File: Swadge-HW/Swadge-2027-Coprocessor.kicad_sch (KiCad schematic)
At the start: 2 parts, among them U6 CH32V003F4U6

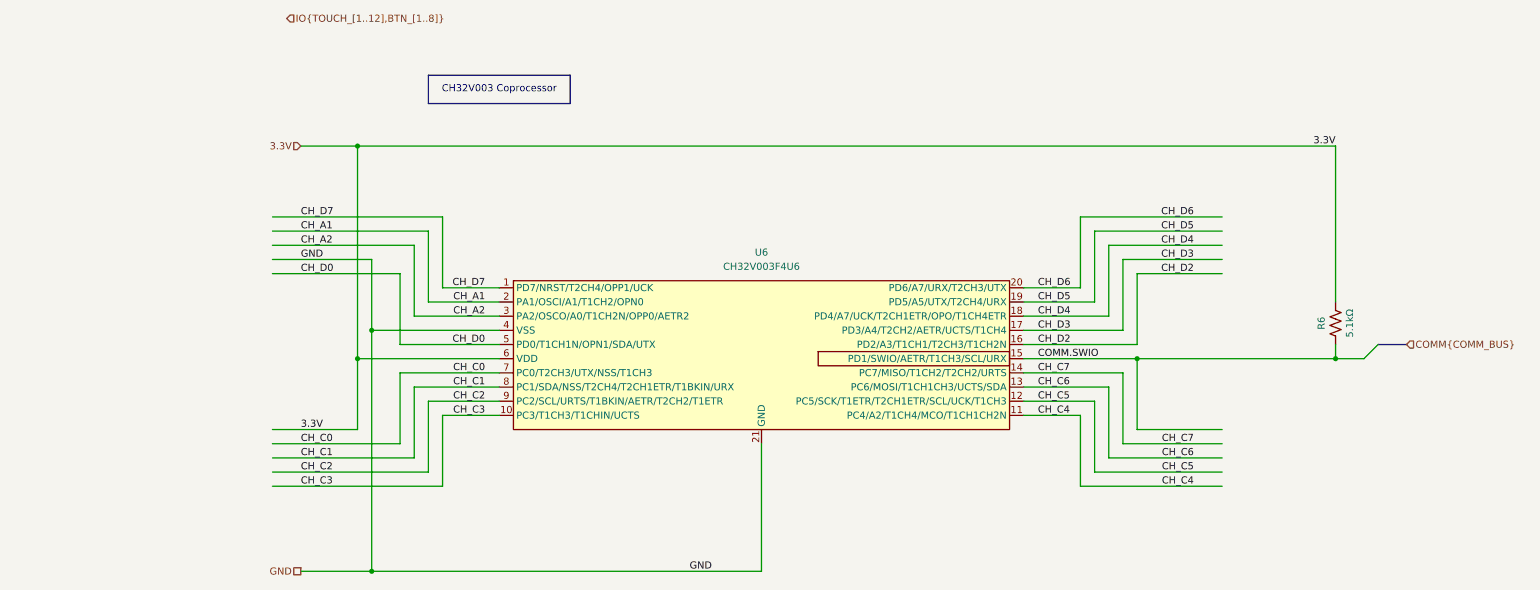
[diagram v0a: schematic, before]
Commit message: Bus Renames
Since we really don't have that many signals I just ditched the bus prefixes and Alias'd them directly.
Added a bus for the interupt and status signals even if they are never used.
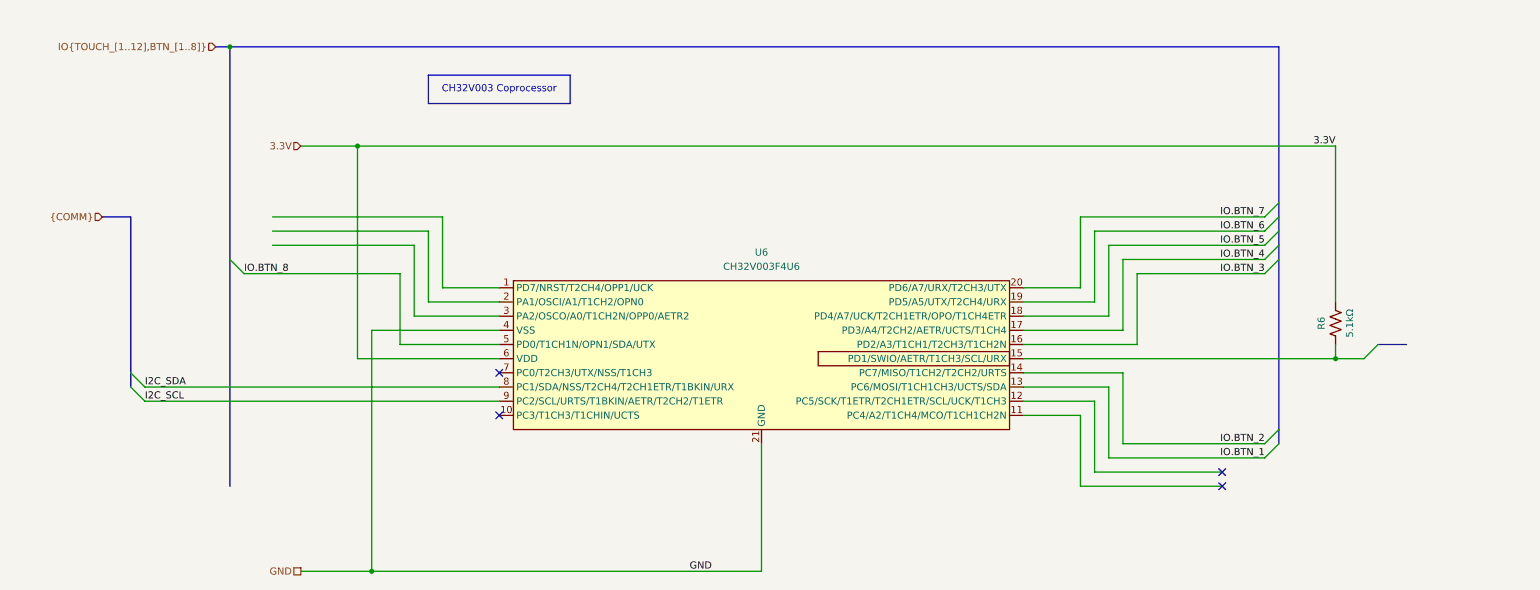
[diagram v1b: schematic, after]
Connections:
- net CH_A1: no longer names the net of U6.2 (PA1/OSCI/A1/T1CH2/OPN0)
- net CH_A2: no longer names the net of U6.3 (PA2/OSCO/A0/T1CH2N/OPP0/AETR2)
- net CH_C0: no longer names the net of U6.7 (PC0/T2CH3/UTX/NSS/T1CH3)
- net CH_C1 renamed I2C_SDA
- net CH_C2 renamed I2C_SCL
- net CH_C3: no longer names the net of U6.10 (PC3/T1CH3/T1CHIN/UCTS)
- net CH_C4: no longer names the net of U6.11 (PC4/A2/T1CH4/MCO/T1CH1CH2N)
- net CH_C5: no longer names the net of U6.12 (PC5/SCK/T1ETR/T2CH1ETR/SCL/UCK/T1CH3)
- net CH_C6 renamed IO.BTN_1
- net CH_C7 renamed IO.BTN_2
- net CH_D0 renamed IO.BTN_8
- net CH_D2 renamed IO.BTN_3
- net CH_D3 renamed IO.BTN_4
- net CH_D4 renamed IO.BTN_5
- net CH_D5 renamed IO.BTN_6
- net CH_D6 renamed IO.BTN_7
- net CH_D7: no longer names the net of U6.1 (PD7/NRST/T2CH4/OPP1/UCK)
- net COMM.SWIO: no longer names the net of R6.1, U6.15 (PD1/SWIO/AETR/T1CH3/SCL/URX)
- no-connect marks 0 -> 4

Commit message: Annotations
Updated Annotations with zonal numbering
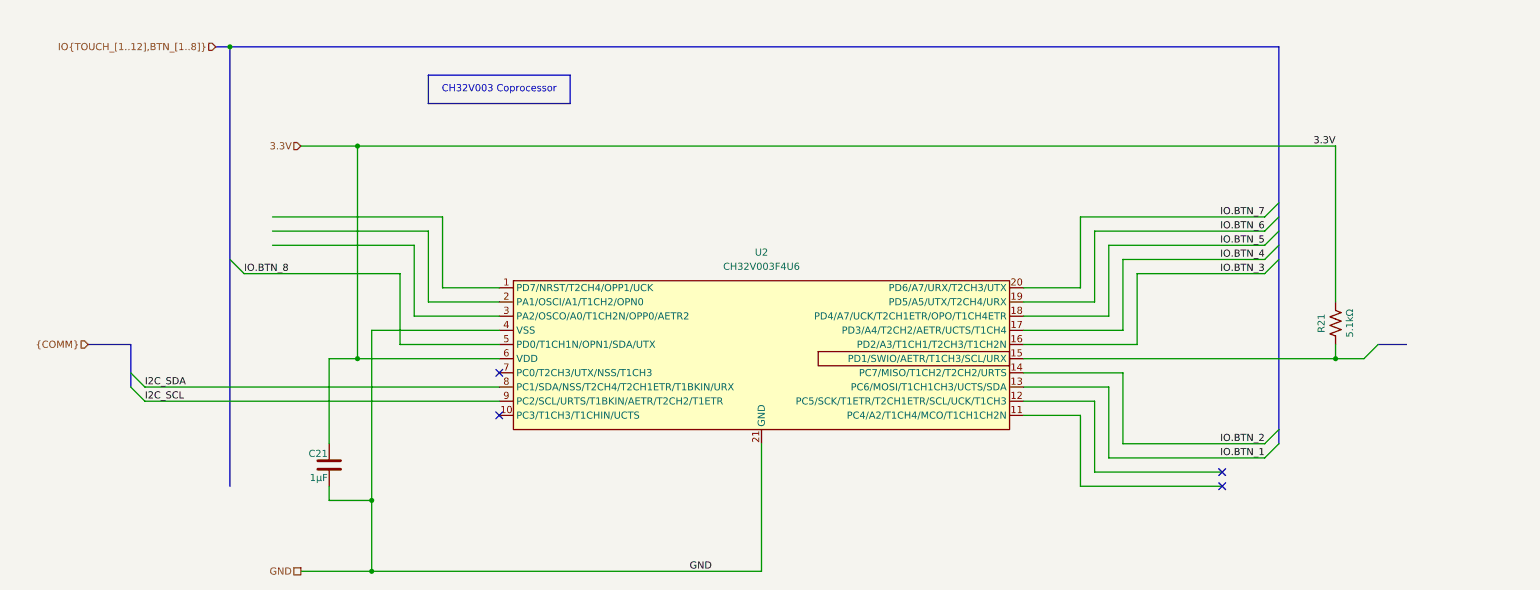
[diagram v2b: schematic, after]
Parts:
- added C21: 1μF, Swadge_Parts:C_0603_1608Metric, symbol Swadge_Parts:C
- renumbered R6 to R21, U6 to U2
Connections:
- net 3.3V: now also C21.1
- net GND: now also C21.2
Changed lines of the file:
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@@
+	)
+	(junction
+		(at 71.12 91.44)
+		(diameter 0)
+		(color 0 0 0 0)
+	)
+	(junction
+		(at 73.66 116.84)
+		(diameter 0)
+		(color 0 0 0 0)
 	)
 	(junction
@@
 	(wire
 		(pts
+			(xy 66.04 91.44) (xy 71.12 91.44)
+		)
+		(stroke
+			(width 0)
+			(type default)
+		)
+	)
+	(wire
+		(pts
 			(xy 208.28 106.68) (xy 233.68 106.68)
 		)
@@
 	(bus
 		(pts
-			(xy 25.4 66.04) (xy 30.48 66.04)
+			(xy 22.86 88.9) (xy 30.48 88.9)
 		)
 		(stroke
@@
 	(wire
 		(pts
-			(xy 73.66 129.54) (xy 73.66 86.36)
+			(xy 73.66 129.54) (xy 73.66 116.84)
+		)
+		(stroke
+			(width 0)
+			(type default)
+		)
+	)
+	(wire
+		(pts
+			(xy 66.04 106.68) (xy 66.04 91.44)
 		)
 		(stroke
@@
 		)
 	)
+	(wire
+		(pts
+			(xy 73.66 116.84) (xy 73.66 86.36)
+		)
+		(stroke
+			(width 0)
+			(type default)
+		)
+	)
+	(wire
+		(pts
+			(xy 66.04 114.3) (xy 66.04 116.84)
+		)
+		(stroke
+			(width 0)
+			(type default)
+		)
+	)
+	(wire
+		(pts
+			(xy 66.04 116.84) (xy 73.66 116.84)
+		)
+		(stroke
+			(width 0)
+			(type default)
+		)
+	)
 	(bus
 		(pts
-			(xy 30.48 66.04) (xy 30.48 93.98)
+			(xy 30.48 88.9) (xy 30.48 93.98)
 		)
 		(stroke
@@
 	(hierarchical_label "{COMM}"
 		(shape input)
-		(at 25.4 66.04 180)
+		(at 22.86 88.9 180)
 		(effects
 			(font
@@
 		(dnp no)
 		(fields_autoplaced yes)
-		(property "Reference" "U6"
+		(property "Reference" "U2"
 			(at 143.51 72.39 0)
 			(show_name no)
@@
 			(project "Swadge-HW"
 				(path "/770c762f-3a30-4864-b7da-de353459cdd6/458cf1f1-40cc-4d0b-81d6-21bbc131062c"
-					(reference "U6")
+					(reference "U2")
+					(unit 1)
+				)
+			)
+		)
+	)
+	(symbol
+		(lib_name "C_13")
+		(lib_id "Swadge_Parts:C")
+		(at 66.04 110.49 0)
+		(mirror y)
+		(unit 1)
+		(body_style 1)
+		(exclude_from_sim no)
+		(in_bom yes)
+		(on_board yes)
+		(in_pos_files yes)
+		(dnp no)
+		(property "Reference" "C21"
+			(at 65.786 108.4579 0)
+			(show_name no)
+			(do_not_autoplace no)
+			(effects
+				(font
+					(size 1.27 1.27)
+				)
+				(justify left)
+			)
+		)
+		(property "Value" "1μF"
+			(at 65.786 112.7759 0)
+			(show_name no)
+			(do_not_autoplace no)
+			(effects
+				(font
+					(size 1.27 1.27)
+				)
+				(justify left)
+			)
+		)
+		(property "Footprint" "Swadge_Parts:C_0603_1608Metric"
+			(at 65.0748 114.3 0)
+			(hide yes)
+			(show_name no)
+			(do_not_autoplace no)
+			(effects
+				(font
+					(size 1.27 1.27)
+				)
+			)
+		)
+		(property "Datasheet" ""
+			(at 66.04 110.49 0)
+			(hide yes)
+			(show_name no)
+			(do_not_autoplace no)
+			(effects
+				(font
+					(size 1.27 1.27)
+				)
+			)
+		)
+		(property "Description" "Unpolarized capacitor"
+			(at 66.04 110.49 0)
+			(hide yes)
+			(show_name no)
+			(do_not_autoplace no)
+			(effects
+				(font
+					(size 1.27 1.27)
+				)
+			)
+		)
+		(property "Digikey" ""
+			(at 62.865 105.41 0)
+			(hide yes)
+			(show_name no)
+			(do_not_autoplace no)
+			(effects
+				(font
+					(size 1.27 1.27)
+				)
+			)
+		)
+		(property "Substitutable" "Y"
+			(at 66.04 110.49 0)
+			(hide yes)
+			(show_name no)
+			(do_not_autoplace no)
+			(effects
+				(font
+					(size 0.001 0.001)
+				)
+			)
+		)
+		(property "LCSC" "C29936"
+			(at 66.04 110.49 0)
+			(hide yes)
+			(show_name no)
+			(do_not_autoplace no)
+			(effects
+				(font
+					(size 1.27 1.27)
+				)
+			)
+		)
+		(pin "2"
+		)
+		(pin "1"
+		)
+		(instances
+			(project "Swadge-HW"
+				(path "/770c762f-3a30-4864-b7da-de353459cdd6/458cf1f1-40cc-4d0b-81d6-21bbc131062c"
+					(reference "C21")
 					(unit 1)
 				)
@@
 		(in_pos_files yes)
 		(dnp no)
-		(property "Reference" "R6"
+		(property "Reference" "R21"
 			(at 243.84 85.09 90)
 			(show_name no)
@@
 			(project "Swadge-HW"
 				(path "/770c762f-3a30-4864-b7da-de353459cdd6/458cf1f1-40cc-4d0b-81d6-21bbc131062c"
-					(reference "R6")
+					(reference "R21")
 					(unit 1)
 				)

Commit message: Starting PCB
Very Rough Initial Layout
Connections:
- no-connect marks 4 -> 7
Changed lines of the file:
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@@
+	)
+	(no_connect
+		(at 55.88 68.58)
+	)
+	(no_connect
+		(at 55.88 71.12)
 	)
 	(no_connect
@@
 	)
 	(no_connect
+		(at 55.88 66.04)
+	)
+	(no_connect

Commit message: major routing changes
Routed SPI
Started Test Routing Touch Inputs
Rough routing for LCD Power
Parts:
- C21: Cost @ 2.5k (none) -> 0.0121
- R21: Cost @ 2.5k 0.0007 -> 0.0023
- U2: Cost @ 2.5k (none) -> 0.1798
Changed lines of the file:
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@@
+			)
+		)
+		(property "Cost @ 2.5k" "0.1798"
+			(at 143.51 90.17 0)
+			(hide yes)
+			(show_name no)
+			(do_not_autoplace no)
+			(effects
+				(font
+					(size 1.27 1.27)
+				)
 			)
 		)
@@
 			)
 		)
+		(property "Cost @ 2.5k" "0.0121"
+			(at 66.04 110.49 0)
+			(hide yes)
+			(show_name no)
+			(do_not_autoplace no)
+			(effects
+				(font
+					(size 1.27 1.27)
+				)
+			)
+		)
 		(pin "2"
 		)
@@
 			)
 		)
-		(property "Cost @ 2.5k" "0.0007"
-			(at 246.38 85.09 0)
-			(hide yes)
+		(property "Cost @ 2.5k" "0.0023"
+			(at 246.38 85.09 0)
+			(hide yes)

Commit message: Reassigned CH32 IO and Initial Button Routing
Rough in Button Routing
Reassigned CH32 IO mapping to better reflect button locations.
Temporarily added the unused interrupts to the CH32 because why not.
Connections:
- net IO.BTN_1: now also U2.1 (PD7/NRST/T2CH4/OPP1/UCK); no longer U2.13 (PC6/MOSI/T1CH1CH3/UCTS/SDA)
- net IO.BTN_2: now also U2.2 (PA1/OSCI/A1/T1CH2/OPN0); no longer U2.14 (PC7/MISO/T1CH2/T2CH2/URTS)
- net IO.BTN_3: now also U2.20 (PD6/A7/URX/T2CH3/UTX); no longer U2.16 (PD2/A3/T1CH1/T2CH3/T1CH2N)
- net IO.BTN_4: now also U2.3 (PA2/OSCO/A0/T1CH2N/OPP0/AETR2); no longer U2.17 (PD3/A4/T2CH2/AETR/UCTS/T1CH4)
- net IO.BTN_6: now also U2.16 (PD2/A3/T1CH1/T2CH3/T1CH2N); no longer U2.19 (PD5/A5/UTX/T2CH4/URX)
- net IO.BTN_7: now also U2.13 (PC6/MOSI/T1CH1CH3/UCTS/SDA); no longer U2.20 (PD6/A7/URX/T2CH3/UTX)
- net IO.BTN_8: now also U2.12 (PC5/SCK/T1ETR/T2CH1ETR/SCL/UCK/T1CH3); no longer U2.5 (PD0/T1CH1N/OPN1/SDA/UTX)
- net SWIO: now reaches R21.1, U2.15 (PD1/SWIO/AETR/T1CH3/SCL/URX)
- new net BMS_INT: U2.14 (PC7/MISO/T1CH2/T2CH2/URTS)
- new net IMU_INT1: U2.19 (PD5/A5/UTX/T2CH4/URX)
- new net RTC_INT: U2.17 (PD3/A4/T2CH2/AETR/UCTS/T1CH4)
- no-connect marks 7 -> 4

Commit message: Change to ESP32-S3-MINI-1
Change U1 to ESP32-S3-MINI-1-N4R2
Update IO Mapping
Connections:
- net CH32_INT: now reaches U2.11 (PC4/A2/T1CH4/MCO/T1CH1CH2N)
- net CH32_TMR1: now reaches U2.5 (PD0/T1CH1N/OPN1/SDA/UTX)
- no-connect marks 4 -> 2
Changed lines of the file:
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@@
-	)
-	(no_connect
-		(at 215.9 114.3)
 	)
 	(no_connect
@@
 	)
 	(no_connect
-		(at 58.42 76.2)
-	)
-	(no_connect
 		(at 96.52 93.98)
 	)
@@
 	)
 	(bus_entry
+		(at 251.46 116.84)
+		(size -2.54 2.54)
+		(stroke
+			(width 0)
+			(type default)
+		)
+	)
+	(bus_entry
 		(at 236.22 73.66)
 		(size -2.54 2.54)
@@
 	)
 	(bus_entry
-		(at 251.46 123.19)
+		(at 251.46 127)
+		(size -2.54 2.54)
+		(stroke
+			(width 0)
+			(type default)
+		)
+	)
+	(bus_entry
+		(at 251.46 121.92)
 		(size -2.54 2.54)
 		(stroke
@@
 	)
 	(bus_entry
-		(at 251.46 127)
+		(at 251.46 124.46)
 		(size -2.54 2.54)
 		(stroke
@@
 		)
 	)
+	(bus
+		(pts
+			(xy 251.46 105.41) (xy 251.46 119.38)
+		)
+		(stroke
+			(width 0)
+			(type default)
+		)
+	)
 	(wire
 		(pts
@@
 	(bus
 		(pts
-			(xy 251.46 123.19) (xy 251.46 127)
+			(xy 251.46 121.92) (xy 251.46 124.46)
 		)
 		(stroke
@@
 	(wire
 		(pts
+			(xy 238.76 129.54) (xy 248.92 129.54)
+		)
+		(stroke
+			(width 0)
+			(type default)
+		)
+	)
+	(wire
+		(pts
 			(xy 66.04 91.44) (xy 71.12 91.44)
 		)
@@
 		)
 	)
+	(bus
+		(pts
+			(xy 251.46 124.46) (xy 251.46 127)
+		)
+		(stroke
+			(width 0)
+			(type default)
+		)
+	)
 	(wire
 		(pts
@@
 	(bus
 		(pts
-			(xy 251.46 105.41) (xy 251.46 119.38)
-		)
-		(stroke
-			(width 0)
-			(type default)
-		)
-	)
-	(bus
-		(pts
 			(xy 48.26 35.56) (xy 48.26 114.3)
 		)
@@
 	(bus
 		(pts
-			(xy 251.46 119.38) (xy 251.46 123.19)
+			(xy 251.46 119.38) (xy 251.46 121.92)
 		)
 		(stroke
@@
 	(wire
 		(pts
-			(xy 238.76 125.73) (xy 248.92 125.73)
+			(xy 238.76 124.46) (xy 248.92 124.46)
 		)
 		(stroke
@@
 	(wire
 		(pts
+			(xy 238.76 119.38) (xy 248.92 119.38)
+		)
+		(stroke
+			(width 0)
+			(type default)
+		)
+	)
+	(wire
+		(pts
 			(xy 66.04 106.68) (xy 66.04 91.44)
 		)
@@
 	(wire
 		(pts
-			(xy 238.76 129.54) (xy 248.92 129.54)
+			(xy 238.76 127) (xy 248.92 127)
 		)
 		(stroke
@@
 		)
 	)
+	(label "CH32_TMR1"
+		(at 58.42 76.2 0)
+		(effects
+			(font
+				(size 1.27 1.27)
+			)
+			(justify left bottom)
+		)
+	)
 	(label "IO.BTN_3"
 		(at 233.68 66.04 180)
@@
 		)
 	)
+	(label "CH32_INT"
+		(at 238.76 129.54 0)
+		(effects
+			(font
+				(size 1.27 1.27)
+			)
+			(justify left bottom)
+		)
+	)
+	(label "CH32_INT"
+		(at 215.9 114.3 180)
+		(effects
+			(font
+				(size 1.27 1.27)
+			)
+			(justify right bottom)
+		)
+	)
 	(label "IMU_INT1"
 		(at 238.76 121.92 0)
@@
 	)
 	(label "BMS_INT"
-		(at 238.76 129.54 0)
+		(at 238.76 127 0)
+		(effects
+			(font
+				(size 1.27 1.27)
+			)
+			(justify left bottom)
+		)
+	)
+	(label "CH32_TMR1"
+		(at 238.76 119.38 0)
 		(effects
 			(font
@@
 	)
 	(label "RTC_INT"
-		(at 238.76 125.73 0)
-		(effects
-			(font
+		(at 238.76 124.46 0)
+		(effects
+			(font
